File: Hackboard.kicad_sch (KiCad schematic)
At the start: 59 parts, among them J1 Conn_01x24, J2 Micro_SD_Card, J3 Conn_01x09, J4 Conn_01x09, J5 Conn_02x02_Counter_Clockwise, J6 USB_C_Receptacle_USB2.0_16P, J7 Barrel_Jack_Switch, J8 Conn_01x22, Q1 NMOS, Q2 NMOS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

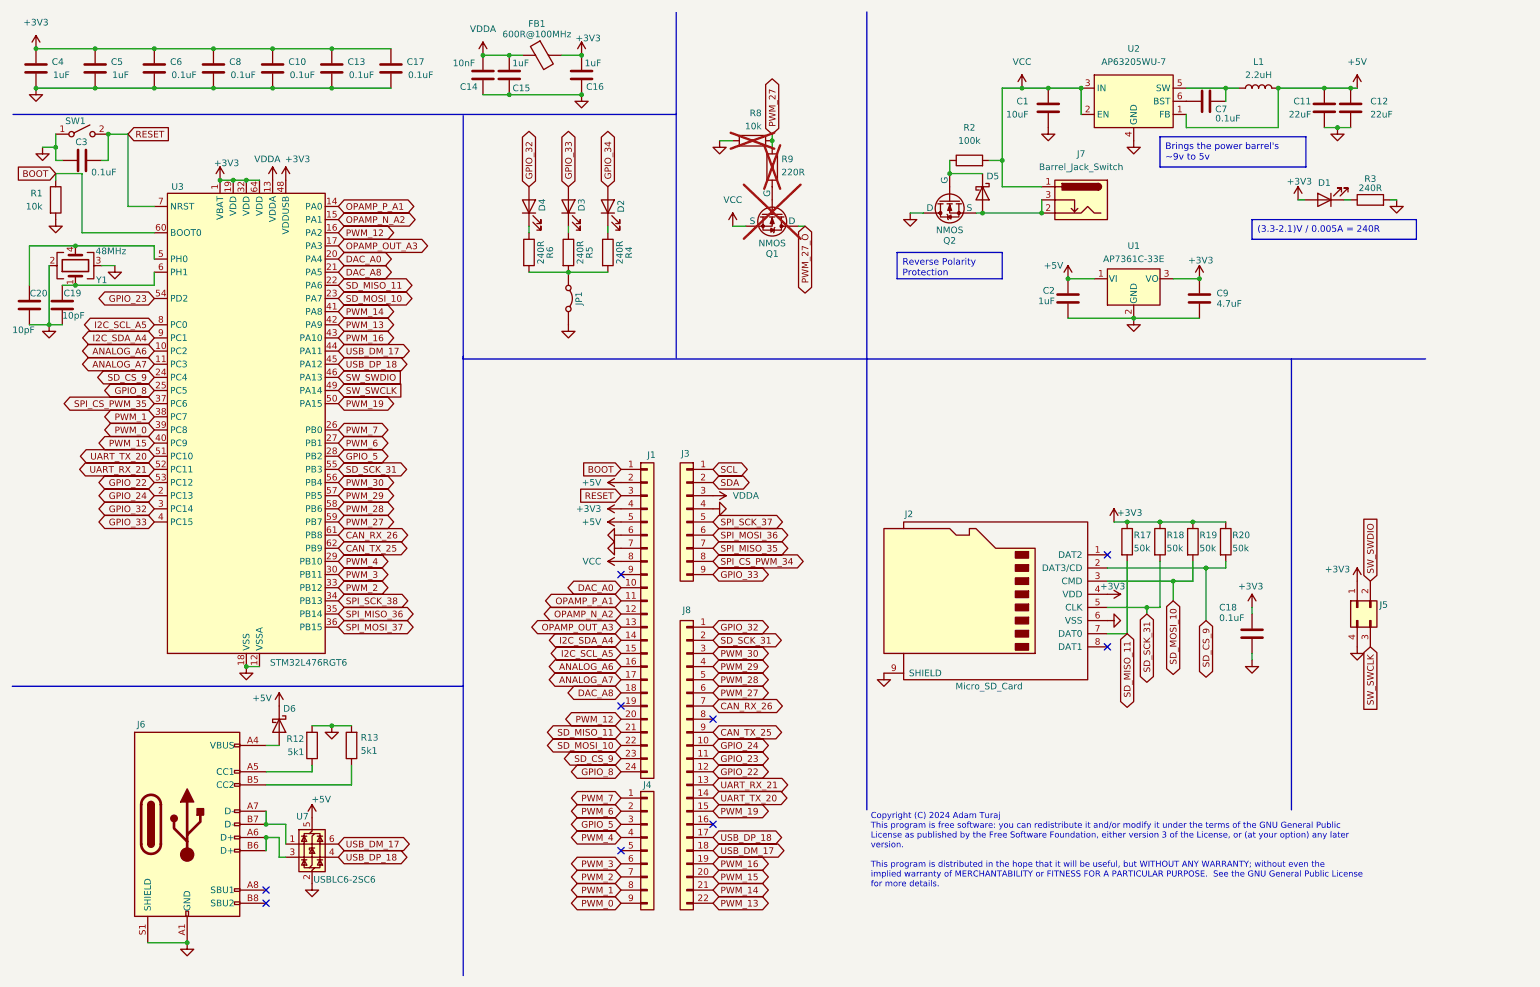
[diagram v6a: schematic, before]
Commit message: Make changes to header, align headers and holes, start tracing
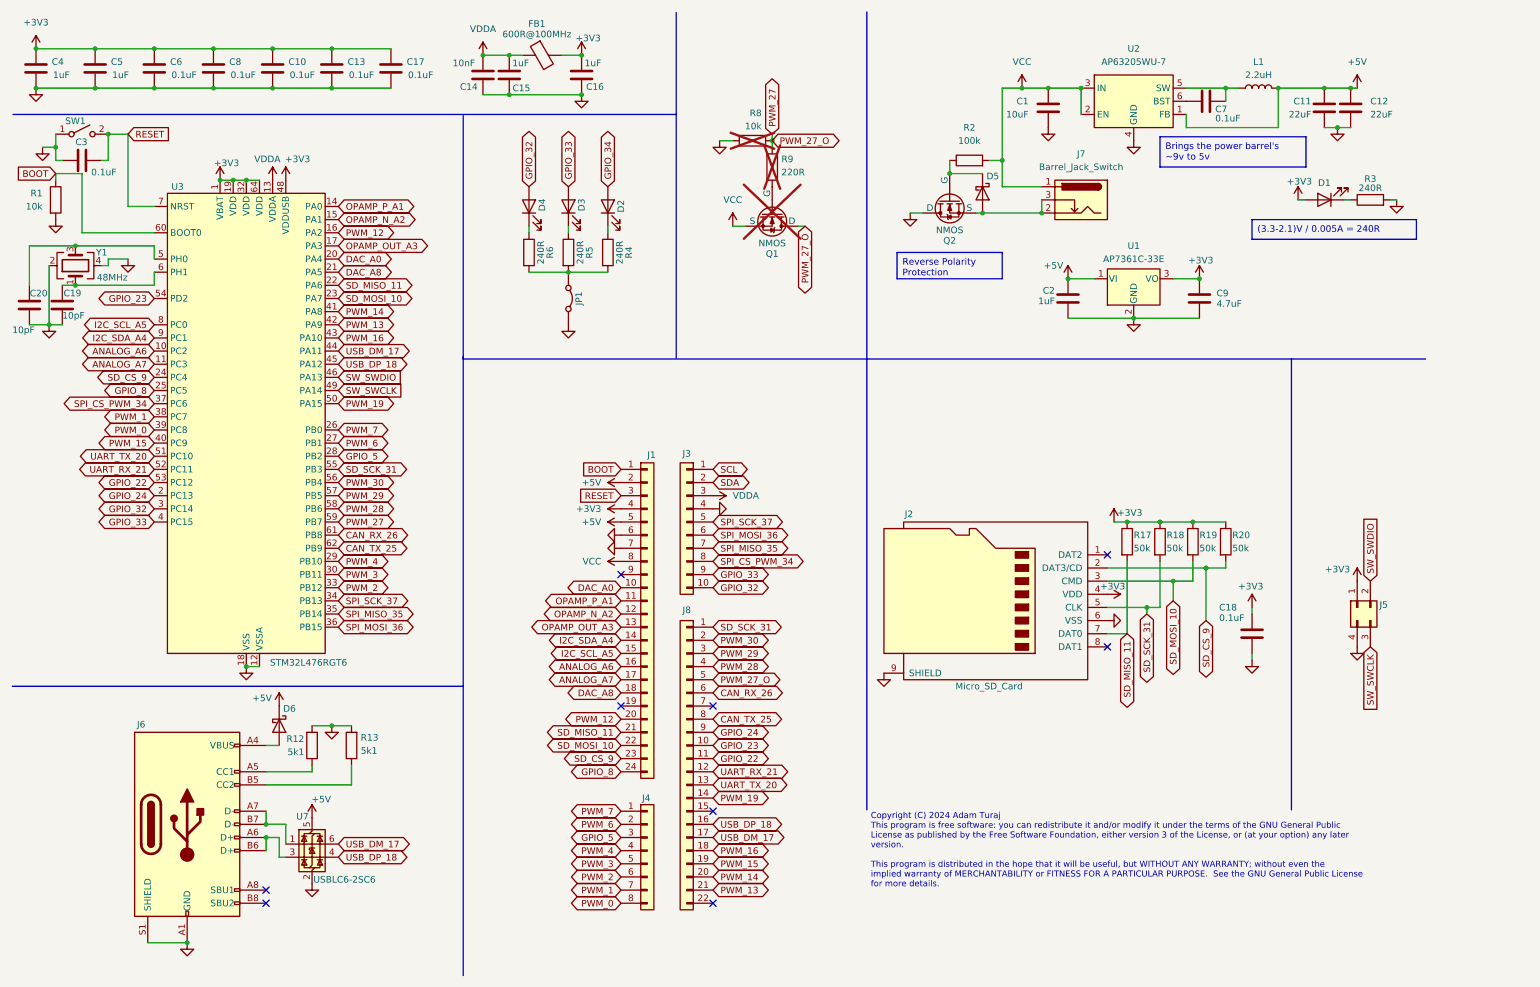
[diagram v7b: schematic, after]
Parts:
- removed J3, J4: Conn_01x09, Headers:PinSocket_1x09_P2.54mm_Vertical, symbol Connector_Generic:Conn_01x09
- removed Y1: 48MHz, Oscillator:Oscillator_SMD_Abracon_ASE-4Pin_3.2x2.5mm_HandSoldering, symbol Device:Crystal_GND23
- added J3: Conn_01x10, Headers:PinSocket_1x10_P2.54mm_Vertical, symbol Connector_Generic:Conn_01x10
- added J4: Conn_01x08, Headers:PinSocket_1x08_P2.54mm_Vertical, symbol Connector_Generic:Conn_01x08
- added Y1: 48MHz, Oscillator:Oscillator_SMD_Abracon_ASE-4Pin_3.2x2.5mm_HandSoldering, symbol Device:Crystal_GND24
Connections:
- net PWM_27_O is gone; now on net PWM_27: Q1.1 (D)
- net SPI_CS_PWM_35 is gone; now on net SPI_CS_PWM_34: U3.37 (PC6)
- net SPI_MISO_36 is gone; now on net SPI_MISO_35: U3.35 (PB14)
- net SPI_MOSI_37 is gone; now on net SPI_MOSI_36: U3.36 (PB15)
- net SPI_SCK_38 is gone; now on net SPI_SCK_37: U3.34 (PB13)
- net CAN_RX_26: now also J8.6 (Pin_6); no longer J8.7 (Pin_7)
- net CAN_TX_25: now also J8.8 (Pin_8); no longer J8.9 (Pin_9)
- net GND: now also J3.4 (Pin_4), Y1.2, Y1.4
- net GPIO_22: now also J8.11 (Pin_11); no longer J8.12 (Pin_12)
- net GPIO_23: now also J8.10 (Pin_10); no longer J8.11 (Pin_11)
- net GPIO_24: now also J8.9 (Pin_9); no longer J8.10 (Pin_10)
- net GPIO_32: now also J3.10 (Pin_10); no longer J8.1 (Pin_1)
- net GPIO_33: now also J3.9 (Pin_9)
- net GPIO_5: now also J4.3 (Pin_3)
- net PWM_0: now also J4.8 (Pin_8)
- net PWM_1: now also J4.7 (Pin_7)
- net PWM_13: now also J8.21 (Pin_21); no longer J8.22 (Pin_22)
- net PWM_14: now also J8.20 (Pin_20); no longer J8.21 (Pin_21)
- net PWM_15: now also J8.19 (Pin_19); no longer J8.20 (Pin_20)
- net PWM_16: now also J8.18 (Pin_18); no longer J8.19 (Pin_19)
- net PWM_19: now also J8.14 (Pin_14); no longer J8.15 (Pin_15)
- net PWM_2: now also J4.6 (Pin_6)
- net PWM_27: now also J8.5 (Pin_5); no longer J8.6 (Pin_6)
- net PWM_28: now also J8.4 (Pin_4); no longer J8.5 (Pin_5)
- net PWM_29: now also J8.3 (Pin_3); no longer J8.4 (Pin_4)
- net PWM_3: now also J4.5 (Pin_5)
- net PWM_30: now also J8.2 (Pin_2); no longer J8.3 (Pin_3)
- net PWM_4: now also J4.4 (Pin_4)
- net PWM_6: now also J4.2 (Pin_2)
- net PWM_7: now also J4.1 (Pin_1)
- net SCL: now also J3.1 (Pin_1)
- net SDA: now also J3.2 (Pin_2)
- net SD_SCK_31: now also J8.1 (Pin_1); no longer J8.2 (Pin_2)
- net SPI_CS_PWM_34: now also J3.8 (Pin_8)
- net SPI_MISO_35: now also J3.7 (Pin_7)
- net SPI_MOSI_36: now also J3.6 (Pin_6)
- net SPI_SCK_37: now also J3.5 (Pin_5)
- net UART_RX_21: now also J8.12 (Pin_12); no longer J8.13 (Pin_13)
- net UART_TX_20: now also J8.13 (Pin_13); no longer J8.14 (Pin_14)
- net USB_DM_17: now also J8.17 (Pin_17); no longer J8.18 (Pin_18)
- net USB_DP_18: now also J8.16 (Pin_16); no longer J8.17 (Pin_17)
- net VDDA: now also J3.3 (Pin_3)
- net at C20.1, U3.5 (PH0): now also Y1.3
- net at C19.1, U3.6 (PH1): now also Y1.1

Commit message: Adjust pinout, start tracing
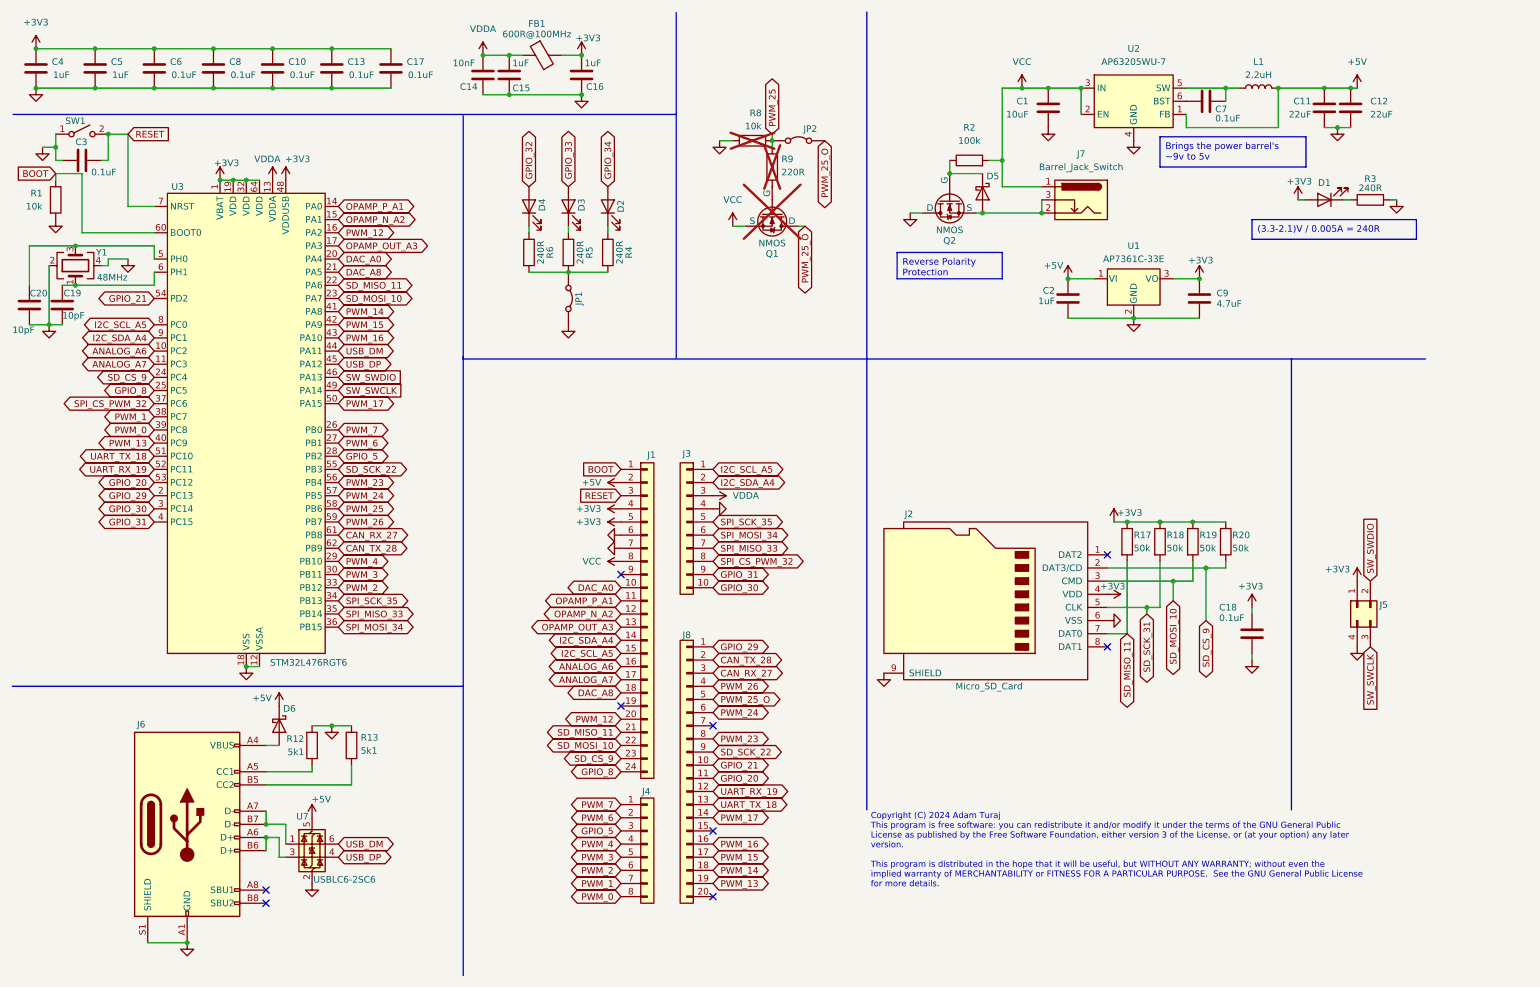
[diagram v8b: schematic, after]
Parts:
- removed J8: Conn_01x22, Headers:PinSocket_1x22_P2.54mm_Vertical, symbol Connector_Generic:Conn_01x22
- added J8: Conn_01x20, Headers:PinSocket_1x20_P2.54mm_Vertical, symbol Connector_Generic:Conn_01x20
- added JP2: Jumper_2_Bridged, Jumper:SolderJumper-2_P1.3mm_Open_RoundedPad1.0x1.5mm, symbol Jumper:Jumper_2_Bridged
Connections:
- net PWM_28 is gone; now on net PWM_25: U3.58 (PB6)
- net SCL is gone; now on net I2C_SCL_A5: J3.1 (Pin_1)
- net SDA is gone; now on net I2C_SDA_A4: J3.2 (Pin_2)
- net +3V3: now also J1.5 (Pin_5)
- net +5V: no longer J1.5 (Pin_5)
- net GPIO_32: no longer J3.10 (Pin_10), U3.3 (PC14)
- net GPIO_33: no longer J3.9 (Pin_9), U3.4 (PC15)
- net PWM_13: now also U3.40 (PC9), J8.19 (Pin_19); no longer U3.42 (PA9)
- net PWM_14: now also J8.18 (Pin_18)
- net PWM_15: now also U3.42 (PA9), J8.17 (Pin_17); no longer U3.40 (PC9)
- net PWM_16: now also J8.16 (Pin_16)
- net SD_SCK_31: no longer U3.55 (PB3)
- net CAN_RX_26 renamed CAN_RX_27
- net CAN_RX_27: now also J8.3 (Pin_3)
- net CAN_TX_25 renamed CAN_TX_28
- net CAN_TX_28: now also J8.2 (Pin_2)
- net GPIO_22 renamed GPIO_20
- net GPIO_20: now also J8.11 (Pin_11)
- net GPIO_23 renamed GPIO_21
- net GPIO_21: now also J8.10 (Pin_10)
- net GPIO_24 renamed GPIO_29
- net GPIO_29: now also J8.1 (Pin_1)
- net PWM_19 renamed PWM_17
- net PWM_17: now also J8.14 (Pin_14)
- net PWM_27 renamed PWM_25
- net PWM_25: now also JP2.1 (A); no longer Q1.1 (D), U3.59 (PB7)
- net PWM_29 renamed PWM_24
- net PWM_24: now also J8.6 (Pin_6)
- net PWM_30 renamed PWM_23
- net PWM_23: now also J8.8 (Pin_8)
- net SPI_CS_PWM_34 renamed SPI_CS_PWM_32
- net SPI_MISO_35 renamed SPI_MISO_33
- net SPI_MOSI_36 renamed SPI_MOSI_34
- net SPI_SCK_37 renamed SPI_SCK_35
- net UART_RX_21 renamed UART_RX_19
- net UART_RX_19: now also J8.12 (Pin_12)
- net UART_TX_20 renamed UART_TX_18
- net UART_TX_18: now also J8.13 (Pin_13)
- net USB_DM_17 renamed USB_DM
- net USB_DP_18 renamed USB_DP
- new net GPIO_30: J3.10 (Pin_10), U3.3 (PC14)
- new net GPIO_31: J3.9 (Pin_9), U3.4 (PC15)
- new net PWM_25_O: J8.5 (Pin_5), JP2.2 (B), Q1.1 (D)
- new net PWM_26: J8.4 (Pin_4), U3.59 (PB7)
- new net SD_SCK_22: J8.9 (Pin_9), U3.55 (PB3)
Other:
- moved on the sheet: J4
